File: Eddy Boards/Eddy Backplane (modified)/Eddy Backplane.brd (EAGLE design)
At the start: 254 x 101.6 mm, 72 parts, among them J1 USB_MINI-B_SMT, P1 39-30-02?_S, P2 RB1-125BAG1A, P3 39-30-04?_S, U1 W5500, U2 STM32F405RGT6, Y2 12MHz, Y3 32.768kHz

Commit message: Updated Copro PWM drivers and programming header
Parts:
- removed R1, R2, R3, R4, R5, R6, R7, R8: 10k, rcl:R0603
- added Q1, Q2, Q3, Q4, Q5, Q6, Q7, Q8: 310mA/60V/1.6Ω, SparkFun-DiscreteSemi:SOT323
- added R25, R26, R28, R29, R31, R32, R33, R34, R35, R36, R37, R38, R39, R40, R41, R42: 10k, rcl:R0603
- added SWDIO/SWDCLK/RESET: (no value), SparkFun-Connectors:2X10
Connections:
- new net PWM_3V3_1: Q1.2, R25.2, U2.61
- new net PWM_3V3_2: Q5.2, R35.2, U2.62
- new net PWM_3V3_3: Q2.2, R28.2, U2.35
- new net PWM_3V3_4: Q6.2, R37.2, U2.36
- new net PWM_3V3_5: Q3.2, R31.2, U2.14
- new net PWM_3V3_6: Q7.2, R39.2, U2.15
- new net PWM_3V3_7: Q4.2, R33.2, U2.16
- new net PWM_3V3_8: Q8.2, R41.2, U2.17
- net +3V3: now also SWDIO/SWDCLK/RESET.1, SWDIO/SWDCLK/RESET.2
- net 3.3V: now also Q1.1, Q2.1, Q3.1, Q4.1, Q5.1, Q6.1, Q7.1, Q8.1, R25.1, R28.1, R31.1, R33.1, R35.1, R37.1, R39.1, R41.1
- net 5V: now also R26.1, R29.1, R32.1, R34.1, R36.1, R38.1, R40.1, R42.1; no longer R1.1, R2.1, R3.1, R4.1, R5.1, R6.1, R7.1, R8.1
- net GND: now also SWDIO/SWDCLK/RESET.10, SWDIO/SWDCLK/RESET.12, SWDIO/SWDCLK/RESET.14, SWDIO/SWDCLK/RESET.16, SWDIO/SWDCLK/RESET.18, SWDIO/SWDCLK/RESET.20, SWDIO/SWDCLK/RESET.4, SWDIO/SWDCLK/RESET.6, SWDIO/SWDCLK/RESET.8
- net PWM_1: now also Q1.3, R26.2; no longer R1.2
- net PWM_2: now also Q5.3, R36.2; no longer R2.2
- net PWM_3: now also Q2.3, R29.2; no longer R3.2
- net PWM_4: now also Q6.3, R38.2; no longer R4.2
- net PWM_5: now also Q3.3, R32.2; no longer R5.2
- net PWM_6: now also Q7.3, R40.2; no longer R6.2
- net PWM_7: now also Q4.3, R34.2; no longer R7.2
- net PWM_8: now also Q8.3, R42.2; no longer R8.2
- net SWCLK: now also SWDIO/SWDCLK/RESET.9
- net SWDIO: now also SWDIO/SWDCLK/RESET.7
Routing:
- net PWM_1: track 213.2 -> 129.3 mm
- net PWM_2: track 212.5 -> 130.6 mm
- net PWM_3: track 211.3 -> 131.9 mm
- net PWM_4: track 208.7 -> 131.9 mm
- net PWM_5: track 206.6 -> 131.9 mm
- net PWM_6: track 204.0 -> 131.9 mm
- net PWM_7: track 201.9 -> 131.9 mm
- net PWM_8: track 196.6 -> 129.1 mm
- net 5V: track 59.2 -> 46.4 mm

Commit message: Routing round 2 started-Flip
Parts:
- removed C7: 0.1 uF, rcl:C0603
- moved Y3 332.8 mm to (307.3, 64.1)
- moved R39 328.2 mm to (297.8, 44.5), turned to 180 degrees
- moved C18 326.1 mm to (316.2, 55.2)
- moved C21 326.1 mm to (304.2, 60.3)
- moved C24 326.1 mm to (304.2, 55.2)
- moved R27 326.1 mm to (327.7, 55.2)
- moved C17 326.1 mm to (310.5, 55.2)
- moved C19 326.1 mm to (318.1, 60.3)
- moved C20 326.1 mm to (324.5, 60.3)
- moved C22 326.1 mm to (311.1, 60.3)
- moved C23 326.1 mm to (330.8, 60.3)
- moved R30 326.1 mm to (321.9, 55.2)
- moved U2 326.1 mm to (311.1, 81.9)
- moved Y2 326.1 mm to (325.8, 67.9)
- moved R40 320.1 mm to (295.3, 41.9), turned to 90 degrees
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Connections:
- net 3.3V: no longer C7.1
- net GND: no longer C7.2
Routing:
- net 3.3V: track 62.4 -> 74.7 mm
- net PWM_1: track 129.3 -> 135.9 mm
- net PWM_8: track 129.1 -> 135.3 mm
- net PWM_6: track 131.9 -> 138.1 mm
- net PWM_4: track 131.9 -> 138.1 mm
- net PWM_3: track 131.9 -> 138.1 mm
- net PWM_7: track 131.9 -> 138.1 mm
- net PWM_5: track 131.9 -> 138.1 mm
- net PWM_2: track 130.6 -> 136.8 mm
- net PWM_3V3_3: track 0.00 -> 3.78 mm
- net PWM_3V3_2: track 0.00 -> 3.78 mm
- net PWM_3V3_1: track 0.00 -> 3.78 mm
- net PWM_3V3_4: track 0.00 -> 3.78 mm
- net PWM_3V3_6: track 0.00 -> 3.69 mm
- net PWM_3V3_8: track 0.00 -> 3.69 mm
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- removed copper zone on layer 16, net ISOLATION

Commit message: Routing began on Eddy backplane. New size
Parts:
- removed 16MHZ, 32.768KHZ: (no value), SparkFun-Clocks:HC49US
- removed C10, C11, C12, C9: (no value), rcl:C0603
- removed C3, C8: 2.2 uF, rcl:C0603
- removed R24: (no value), rcl:R0603
- removed U$4: STM32F405RGT6, SparkFun-IC-Microcontroller:TQFP64
- added C25, C26, C27, C7: (no value), rcl:C0603
- added R1, R2, R3, R5, R6: (no value), rcl:R0603
- moved P1 244.4 mm to (5.71, 106.0), turned to 180 degrees
- moved SWITCH_CONNECTOR 214.3 mm to (27.2, 106.4), turned to 180 degrees
- moved R23 205.7 mm to (94.5, 115.3), turned to 270 degrees
- moved C23 202.7 mm to (133.3, 105.8), turned to 180 degrees
- moved R27 200.9 mm to (134.7, 111.5)
- moved U$6 198.3 mm to (63.8, 116.8)
- moved C19 195.5 mm to (124.5, 87.0), turned to 90 degrees
- moved Y2 191.6 mm to (137.2, 101.5)
- moved P3 187.8 mm to (50.9, 105.2), turned to 180 degrees
- moved C20 187.8 mm to (138.6, 86.5), turned to 180 degrees
- moved U$8 187.5 mm to (63.6, 110.6)
- moved R9 186.7 mm to (67.9, 104.0), turned to 270 degrees
- moved C17 185.7 mm to (130.6, 101.0), turned to 90 degrees
- moved R30 184.9 mm to (141.2, 94.5), turned to 270 degrees
- moved C18 184.3 mm to (138.7, 104.5), turned to 180 degrees
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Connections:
- removed net N$1: C3.1, U$4.31
- removed net N$2: C8.1, U$4.47
- removed net N$3: 32.768KHZ.1, C11.1, U$4.3
- removed net N$5: 16MHZ.1, C9.1, U$4.5
- removed net N$6: 32.768KHZ.2, C12.1, U$4.4
- removed net N$7: 16MHZ.2, C10.1, U$4.6
- new net N$22: C25.2, R5.2, R6.2
- new net N$23: P2.R1, R3.2, U1.2
- new net N$24: P2.R2, R2.2, U1.1
- new net N$25: C26.2, P2.R7
- new net N$26: C26.1, R5.1, U1.6
- new net N$27: C27.2, R6.1, U1.5
- new net N$28: C27.1, P2.R8
- net +3V3: now also C1.1, C2.1, C4.1, C5.1, C6.1, C7.1, P2.R3, Q1.1, Q2.1, Q3.1, Q4.1, Q5.1, Q6.1, Q7.1, Q8.1, R1.2, R2.1, R23.2, R25.1, R28.1, R3.1, R31.1, R33.1, R35.1, R37.1, R39.1, R41.1
- net 3.3V: no longer C1.1, C2.1, C4.1, C5.1, C6.1, Q1.1, Q2.1, Q3.1, Q4.1, Q5.1, Q6.1, Q7.1, Q8.1, R25.1, R28.1, R31.1, R33.1, R35.1, R37.1, R39.1, R41.1, U$4.13, U$4.19, U$4.32, U$4.48, U$4.64
- net GND: now also C25.1, C7.2; no longer C10.2, C11.2, C12.2, C3.2, C8.2, C9.2, P2.L2, P2.L4, U$4.12, U$4.18, U$4.63
- net KILL_SWITCH: now also SWITCH_CONNECTOR.4; no longer SWITCH_CONNECTOR.2
- net N$11: now also P2.L4; no longer R24.2
- net N$12: now also P2.L2; no longer R23.2
- net N$16: now also R1.1; no longer R24.1
- net SWITCH_2: now also SWITCH_CONNECTOR.2; no longer SWITCH_CONNECTOR.4
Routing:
- net SPARE5: track 223.9 -> 97.2 mm, vias 0 -> 1
- net SPARE6: track 221.3 -> 97.2 mm, vias 0 -> 1
- net 3.3V_ON/OFF: track 211.8 -> 97.2 mm
- net 5V_ON/OFF: track 209.3 -> 97.2 mm
- net ROBOT_SDA: track 212.7 -> 109.2 mm, vias 0 -> 1
- net ROBOT_SCL: track 211.3 -> 108.7 mm, vias 0 -> 1
- net SPARE3: track 197.5 -> 97.2 mm, vias 0 -> 1
- net SPARE2: track 194.8 -> 97.2 mm
- net SPARE7: track 194.7 -> 97.2 mm
- net SPARE4: track 192.4 -> 97.2 mm, vias 0 -> 1
- net ACOUSTIC_ON/OFF: track 181.4 -> 97.2 mm
- net BACKPLANE_SCL: track 207.6 -> 125.7 mm, vias 0 -> 1
- net BACKPLANE_SDA: track 202.5 -> 126.8 mm, vias 0 -> 3
- net 3.3V: track 74.7 -> 0.00 mm, vias 8 -> 0
- net JETSON_ON/OFF: track 204.9 -> 143.6 mm, vias 0 -> 1
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- added copper zone on layer 16, net ISOLATION
- added copper zone on layer 1, net N$1
- added copper zone on layer 1, net N$2
- added copper zone on layer 16, net N$3
- added copper zone on layer 16, net N$5
- added copper zone on layer 16, net N$6
- removed copper zone on layer 1, net 3.3V
- removed copper zone on layer 1, net 5V
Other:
- board size 254 x 101.6 mm -> 154.2 x 120.7 mm
- board text added: "How thick are our boards?"
- board text added: "Questions to ask:"
- board text added: "What size are the radii?"

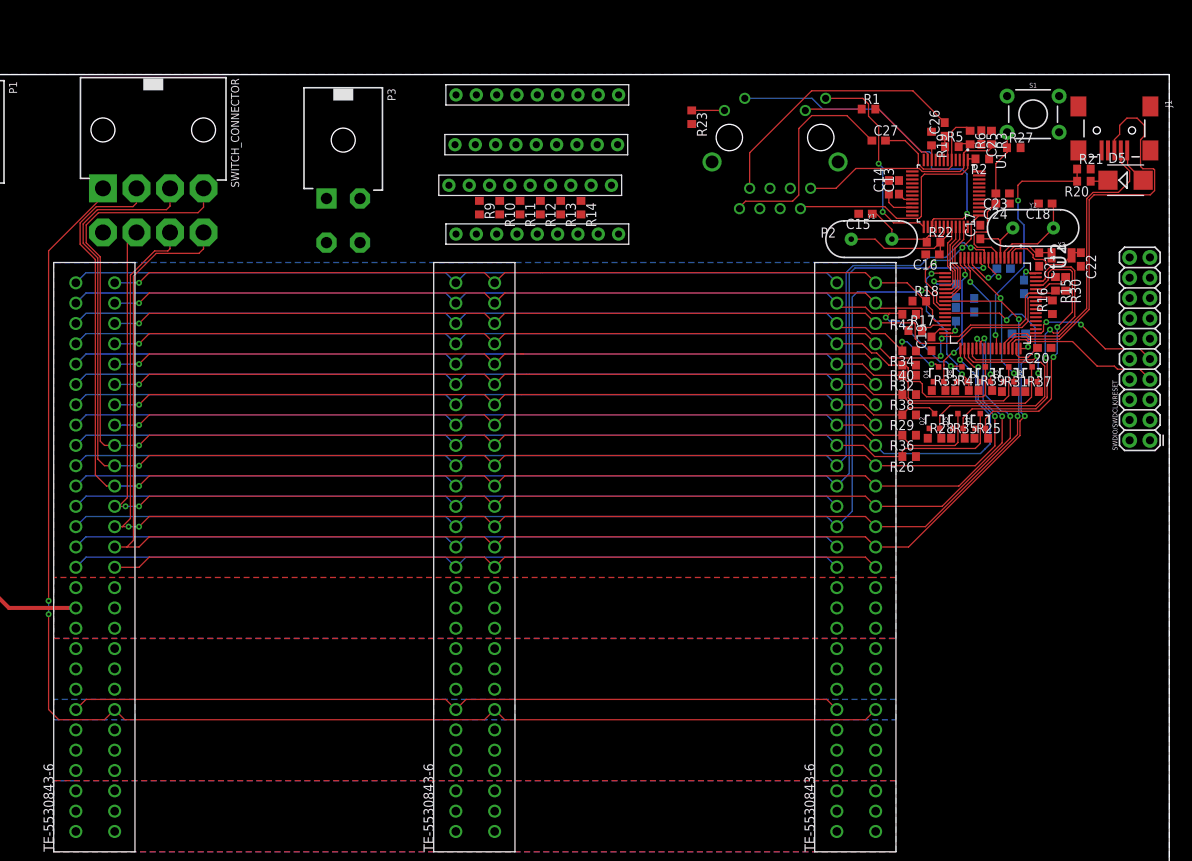
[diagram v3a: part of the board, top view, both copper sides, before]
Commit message: further routing done on Copro/backplane
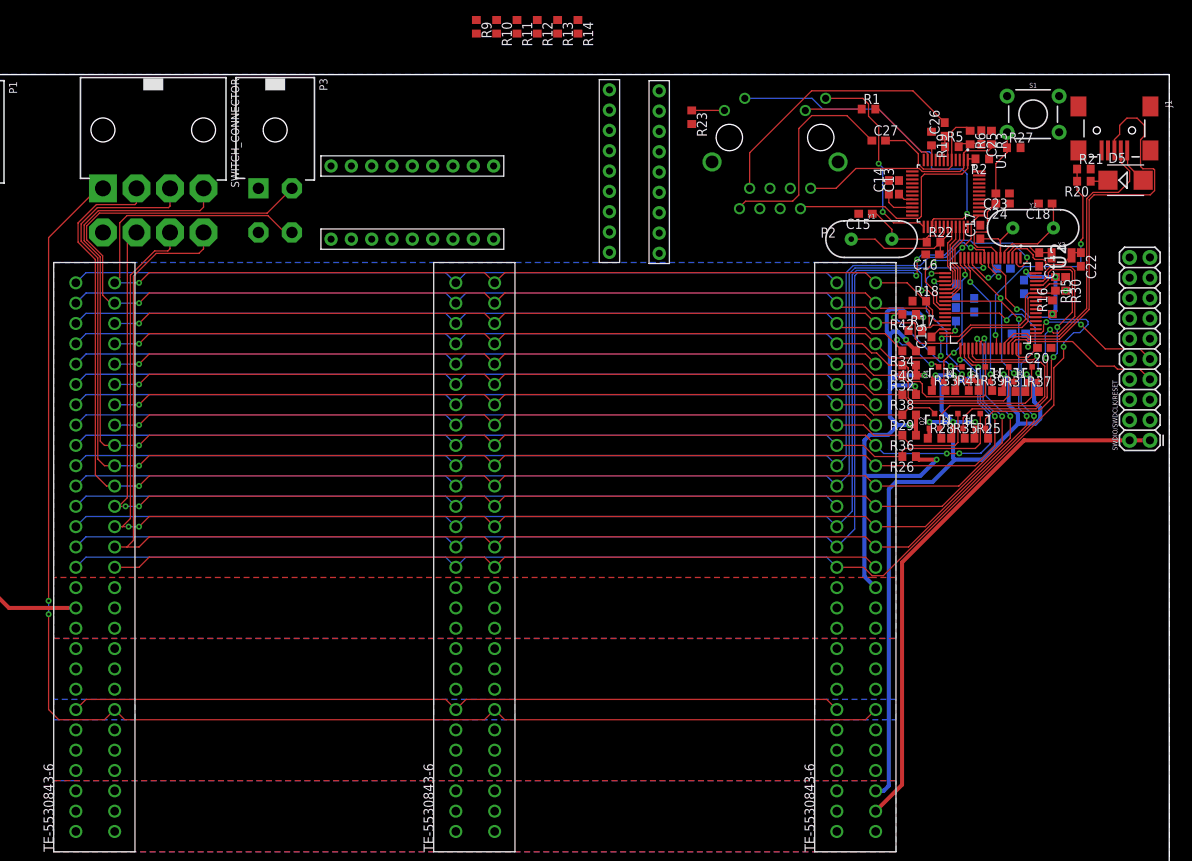
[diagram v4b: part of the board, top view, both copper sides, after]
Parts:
- moved PWR_ON 38.7 mm to (48.1, 98.8), turned to 0 degrees
- moved SWITCH_CONN 28.0 mm to (91.7, 97.0), turned to 90 degrees
- moved U$8 25.7 mm to (85.5, 97.2), turned to 90 degrees
- moved R10 22.6 mm to (70.1, 126.6)
- moved R11 22.6 mm to (72.6, 126.6)
- moved R12 22.6 mm to (75.2, 126.6)
- moved R13 22.6 mm to (77.7, 126.6)
- moved R14 22.6 mm to (80.3, 126.6)
- moved R9 22.6 mm to (67.6, 126.6)
- moved U$6 9.63 mm to (71.0, 110.5), turned to 180 degrees
- moved P3 8.60 mm to (42.4, 106.4)
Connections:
- removed net +3V3: C1.1, C2.1, C23.1, C24.1, C4.1, C5.1, C6.1, C7.1, P2.R3, Q1.1, Q2.1, Q3.1, Q4.1, Q5.1, Q6.1, Q7.1, Q8.1, R1.2, R2.1, R23.2, R25.1, R27.2, R28.1, R3.1, R31.1, R33.1, R35.1, R37.1, R39.1, R41.1, SWDIO/SWDCLK/RESET.1, SWDIO/SWDCLK/RESET.2, U1.11, U1.15, U1.17, U1.21, U1.28, U1.4, U1.8, U2.13, U2.19, U2.32, U2.48, U2.64
- net 3.3V: now also C1.1, C2.1, C23.1, C24.1, C4.1, C5.1, C6.1, C7.1, P2.R3, Q1.1, Q2.1, Q3.1, Q4.1, Q5.1, Q6.1, Q7.1, Q8.1, R1.2, R2.1, R23.2, R25.1, R27.2, R28.1, R3.1, R31.1, R33.1, R35.1, R37.1, R39.1, R41.1, SWDIO/SWDCLK/RESET.1, SWDIO/SWDCLK/RESET.2, U1.11, U1.15, U1.17, U1.21, U1.28, U1.4, U1.8, U2.13, U2.19, U2.32, U2.48, U2.64
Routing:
- net 3.3V: track 0.00 -> 211.2 mm, vias 0 -> 15
- net 5V: track 64.4 -> 143.2 mm, vias 0 -> 6
- net 3.3V_ON/OFF: track 97.2 -> 163.7 mm, vias 0 -> 2
- net 5V_ON/OFF: track 97.2 -> 160.8 mm, vias 0 -> 3
- net ROBOT_SDA: track 109.2 -> 148.6 mm
- net ROBOT_SCL: track 108.7 -> 139.6 mm
- net +3V3: track 27.1 -> 0.00 mm, vias 5 -> 0
- net 12V_ON/OFF: track 140.2 -> 145.1 mm
- net PWM_7: track 113.9 -> 115.1 mm
- net PWM_8: track 118.8 -> 117.8 mm
- net SWITCH_5: track 194.8 -> 195.8 mm
- net SWITCH_4: track 184.6 -> 185.4 mm
- net KILL_SWITCH: track 173.7 -> 174.4 mm, vias 2 -> 4
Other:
- board text added: "Yo we could prob fit the battery balancer board on here too"
- board text removed: "How thick are our boards?"
- board text removed: "Questions to ask:"
- board text removed: "What size are the radii?"
